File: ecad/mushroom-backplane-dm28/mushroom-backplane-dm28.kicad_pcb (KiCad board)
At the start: 2 copper layers, 24 x 63 mm, 20 parts, among them J1 BUSOUT, J2 BUSIN, J3 BACKPLANE, M1 KK 254, Q1 AO3400A, Q2 SI2301CDS-T1-GE3, U1 DM28

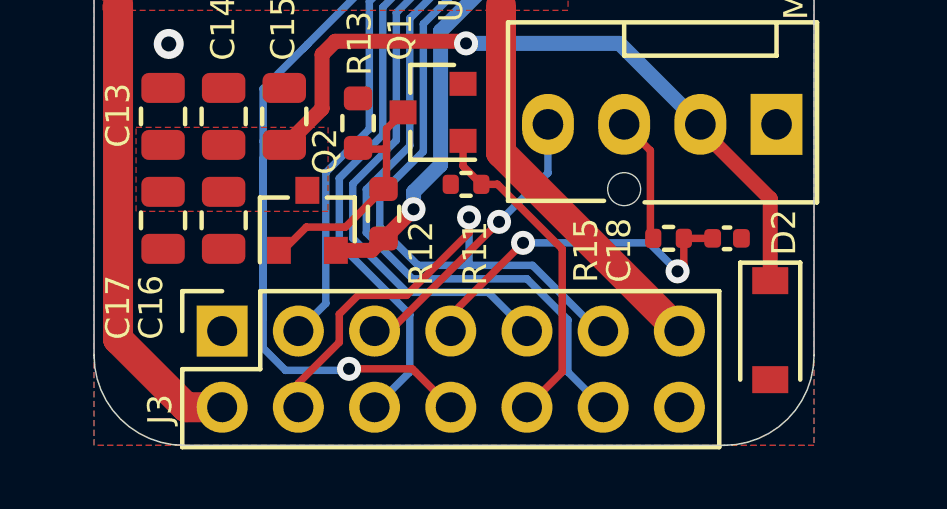
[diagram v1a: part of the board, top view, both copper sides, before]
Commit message: Align pin numbering of backplane and blade
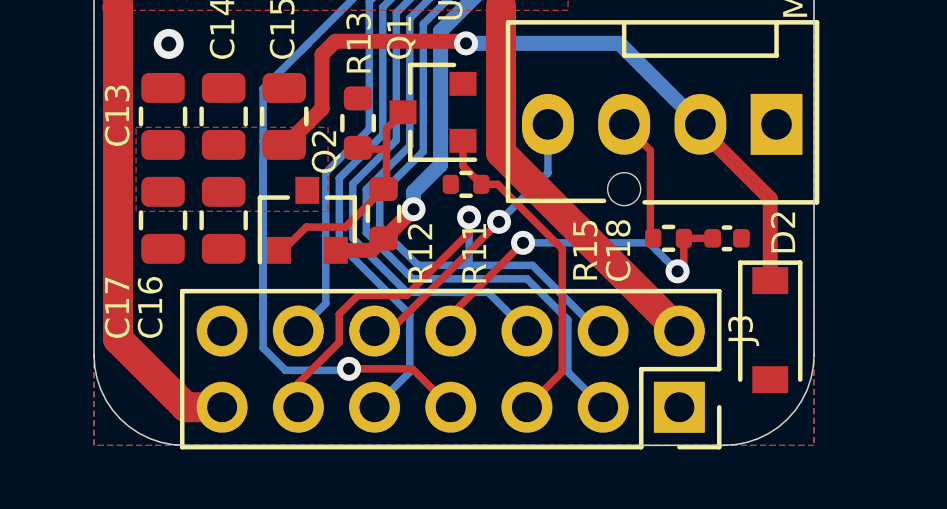
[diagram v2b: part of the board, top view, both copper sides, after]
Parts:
- moved J3 15.5 mm to (107.5, 130.2), turned to 270 degrees
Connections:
- J3 pad 10: FANDCC -> FANPWM
- J3 pad 12: SCL -> SDA
- J3 pad 3: SDA -> SCL
- J3 pad 5: FANPWM -> FANDCC
- J3 pad 6: STX -> SRX
- J3 pad 7: FANFDB -> POWTMP
- J3 pad 8: POWTMP -> FANFDB
- J3 pad 9: SRX -> STX
